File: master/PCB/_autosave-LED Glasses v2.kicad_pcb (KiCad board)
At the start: 2 copper layers, 152.9 x 54.6 mm, 85 parts, among them J1 Conn_01x01_Male, J2 Conn_01x01_Male, J3 Conn_01x01_Male, J4 Conn_01x01_Male, J5 Conn_01x01_Male

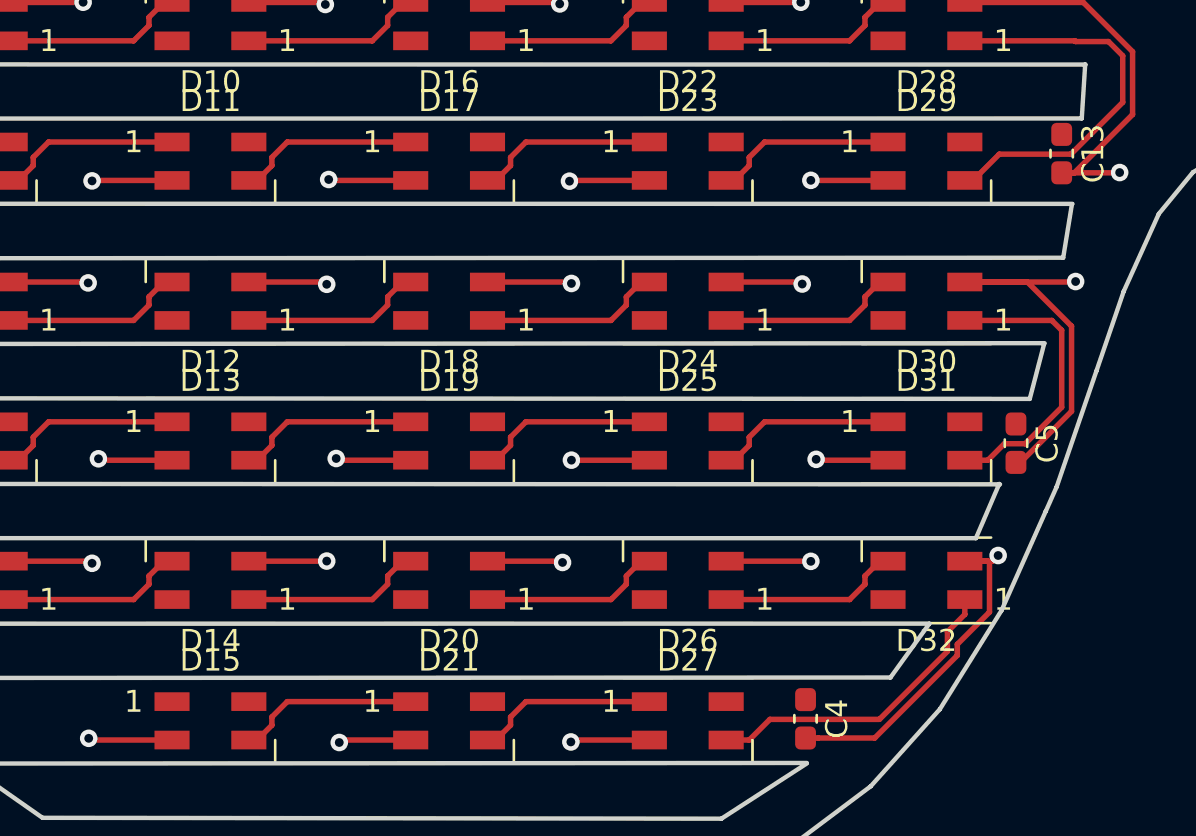
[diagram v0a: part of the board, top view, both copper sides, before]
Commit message: Moved left breakout pads
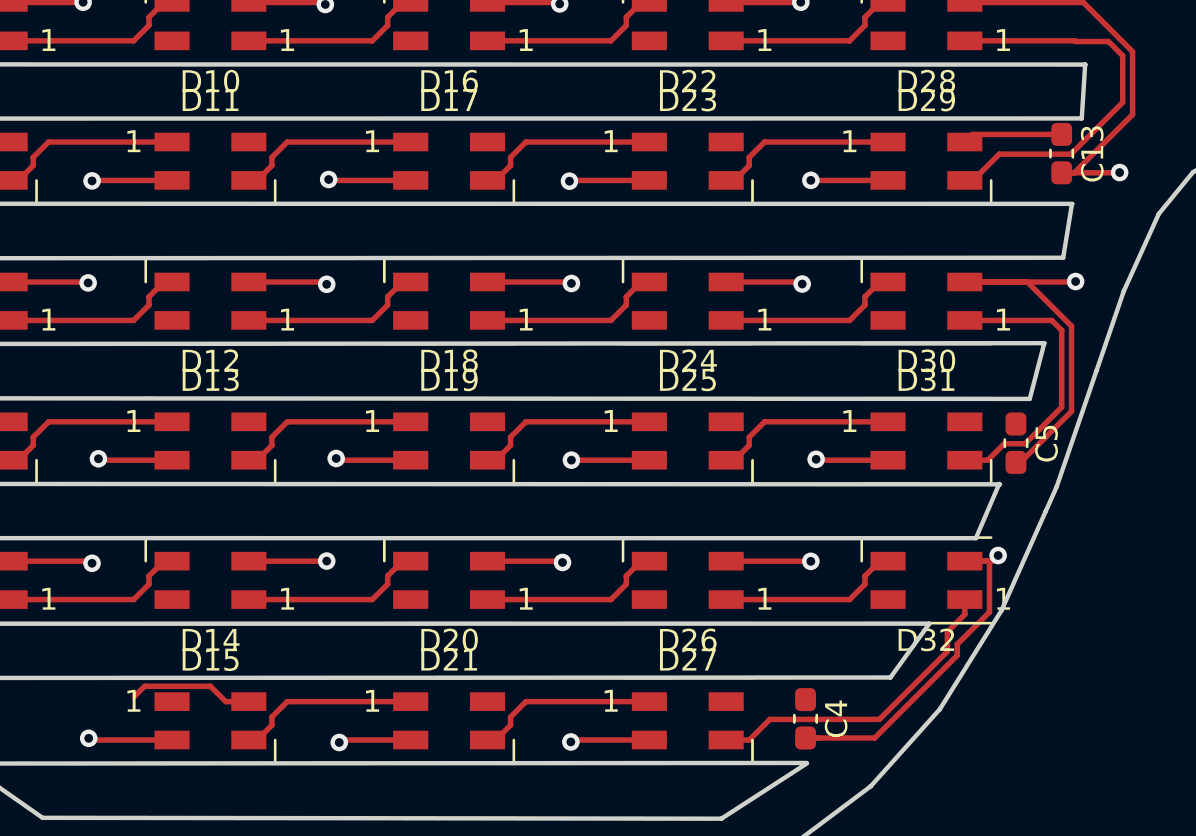
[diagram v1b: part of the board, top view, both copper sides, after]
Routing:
- net Net-(C1-Pad1): track 0.00 -> 10.3 mm
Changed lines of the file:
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@@
     (thickness 1.6)
     (drawings 156)
-    (tracks 606)
+    (tracks 612)
     (zones 0)
     (modules 85)
@@
   (segment (start 221.2 101.225) (end 220.20229 102.22271) (width 0.25) (layer F.Cu) (net 1))
   (segment (start 222.25 101.225) (end 221.2 101.225) (width 0.25) (layer F.Cu) (net 1))
+  (segment (start 147.5963 100.8787) (end 147.25 101.225) (width 0.25) (layer F.Cu) (net 2))
+  (segment (start 151.6634 100.8787) (end 147.5963 100.8787) (width 0.25) (layer F.Cu) (net 2))
+  (segment (start 112.874999 126.024999) (end 109.877501 126.024999) (width 0.25) (layer F.Cu) (net 2))
+  (segment (start 114.625 126.725) (end 113.575 126.725) (width 0.25) (layer F.Cu) (net 2))
+  (segment (start 113.575 126.725) (end 112.874999 126.024999) (width 0.25) (layer F.Cu) (net 2))
+  (segment (start 109.877501 126.024999) (end 109.4105 126.492) (width 0.25) (layer F.Cu) (net 2))
   (segment (start 219.4394 115.725) (end 219.3671 115.7973) (width 0.25) (layer F.Cu) (net 3))
   (segment (start 222.25 115.725) (end 219.4394 115.725) (width 0.25) (layer F.Cu) (net 3))
